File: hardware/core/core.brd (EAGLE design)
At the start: 159.7 x 189.2 mm, 710 parts, among them IC1 MAX481CSA, IC10 MAX481CSA, IC11 MAX481CSA, IC12 MAX481CSA, IC13 MAX481CSA, IC14 MAX481CSA, IC15 MAX481CSA, IC16 MAX481CSA, IC17 MAX481CSA, IC18 MAX481CSA, IC19 MAX481CSA, IC2 LD117AS12TR, IC20 MAX481CSA, IC21 MAX481CSA, IC22 LD117AS12TR, IC3 MAX481CSA, IC4 MAX481CSA, IC5 MAX481CSA, IC6 MAX481CSA, IC7 MAX481CSA, IC8 MAX481CSA, IC9 MAX481CSA, U1 6N138SDM

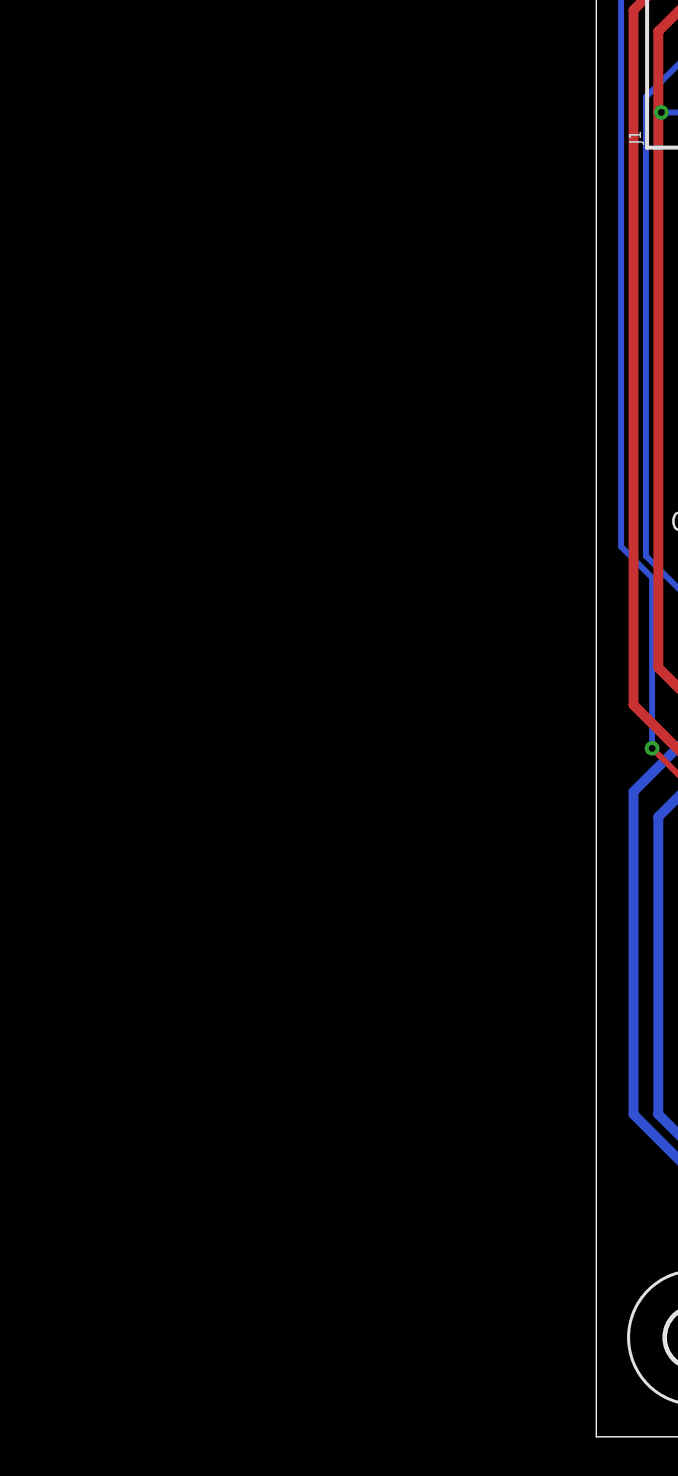
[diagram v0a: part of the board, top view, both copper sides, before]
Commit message: add esp32-s3
(for future use)
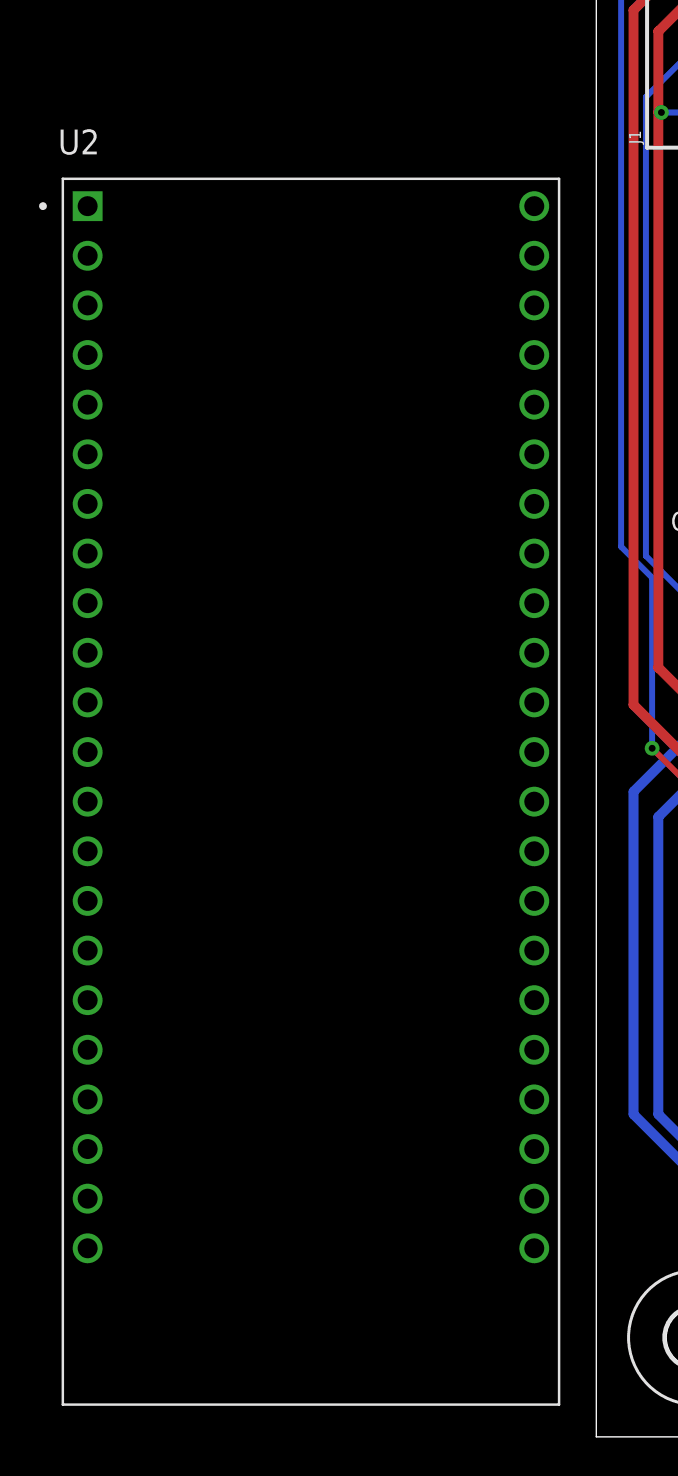
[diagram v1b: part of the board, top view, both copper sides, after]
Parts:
- added U2: ESP32-S3-DEVKITC-1-N8R2, ESP32-S3-DEVKITC-1-N8R2:XCVR_ESP32-S3-DEVKITC-1-N8R2
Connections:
- new net 3V3: U2.J1_1, U2.J1_2
- new net 5V0: U2.J1_21
- net GND: now also U2.J1_22, U2.J3_1, U2.J3_21, U2.J3_22

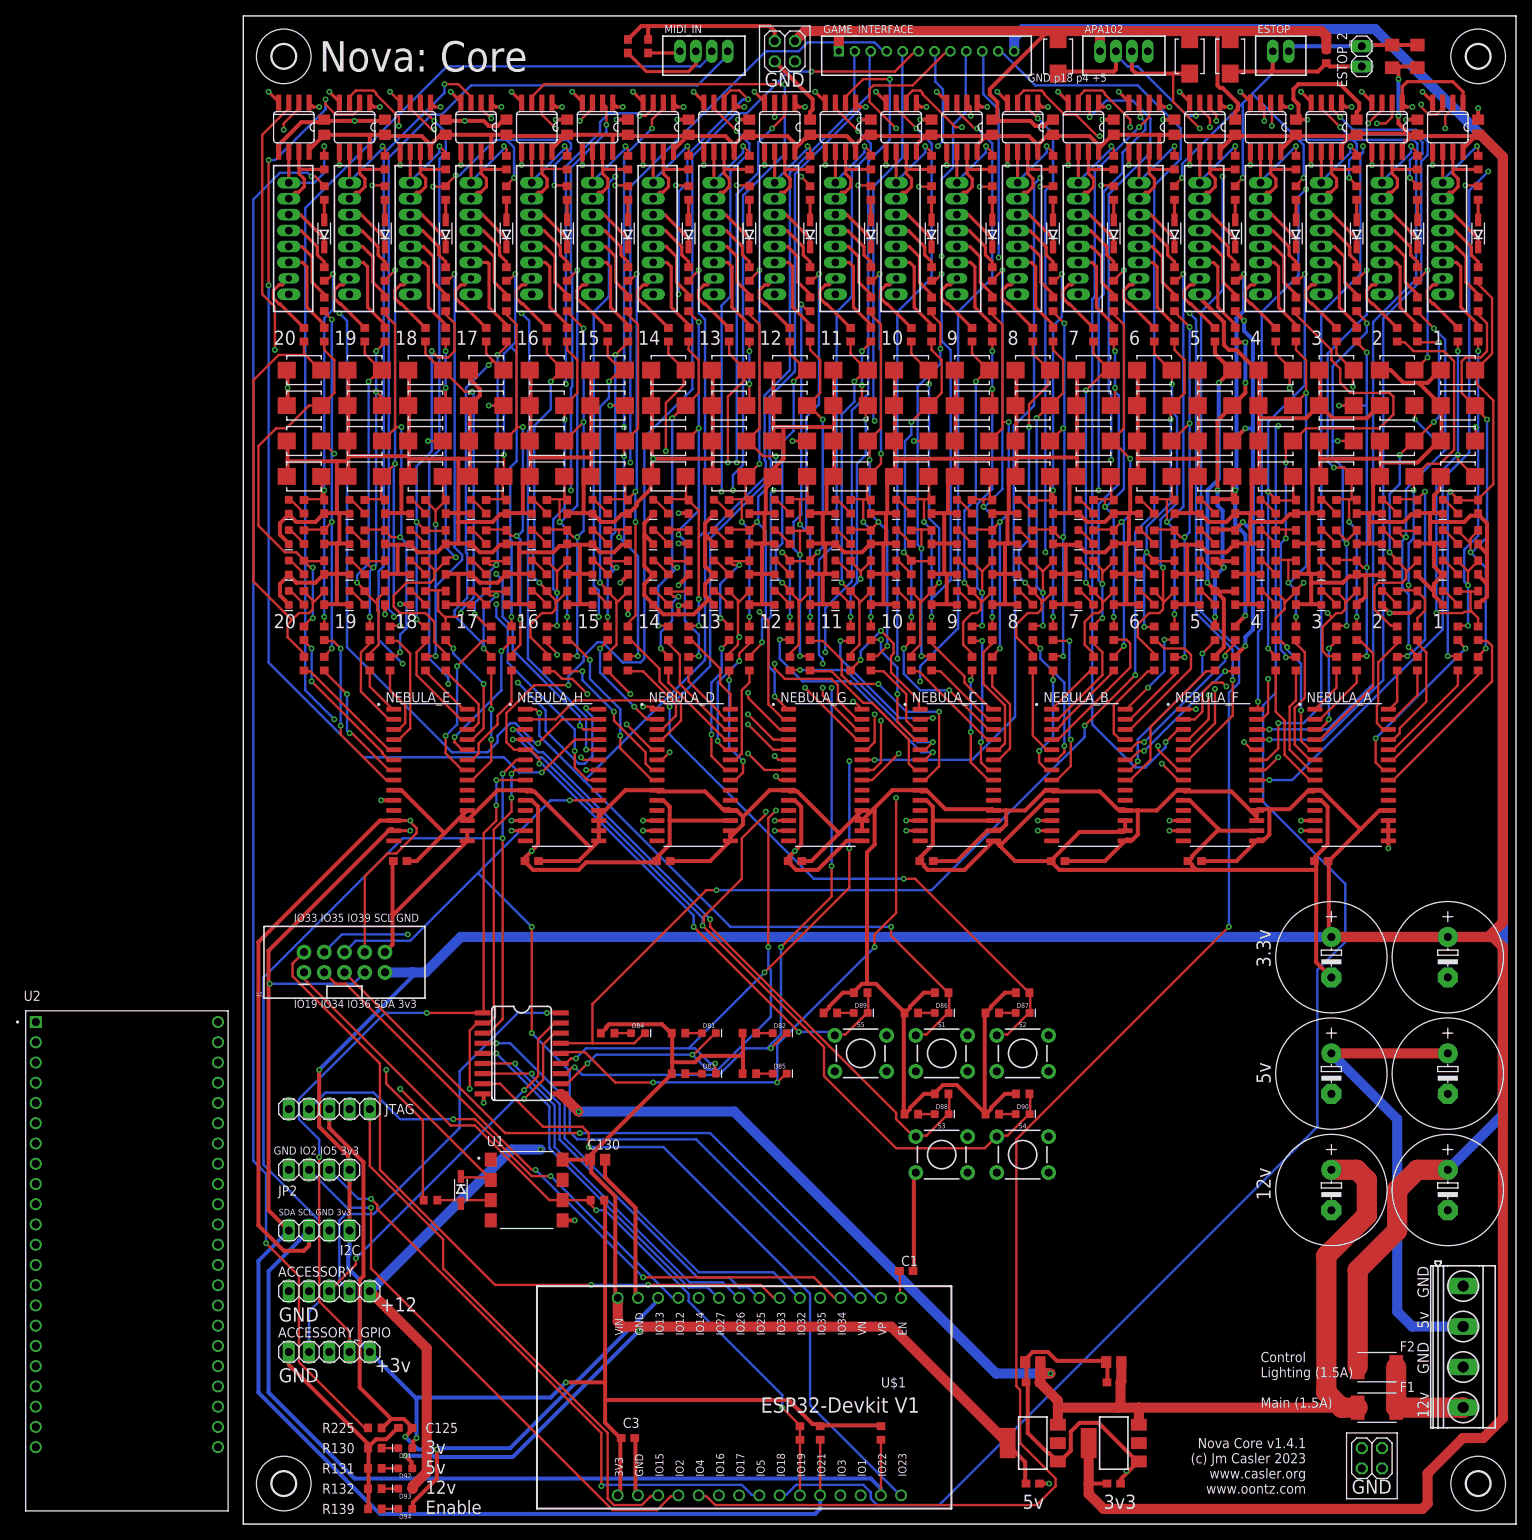
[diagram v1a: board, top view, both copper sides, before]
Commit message: re & de status LEDs added
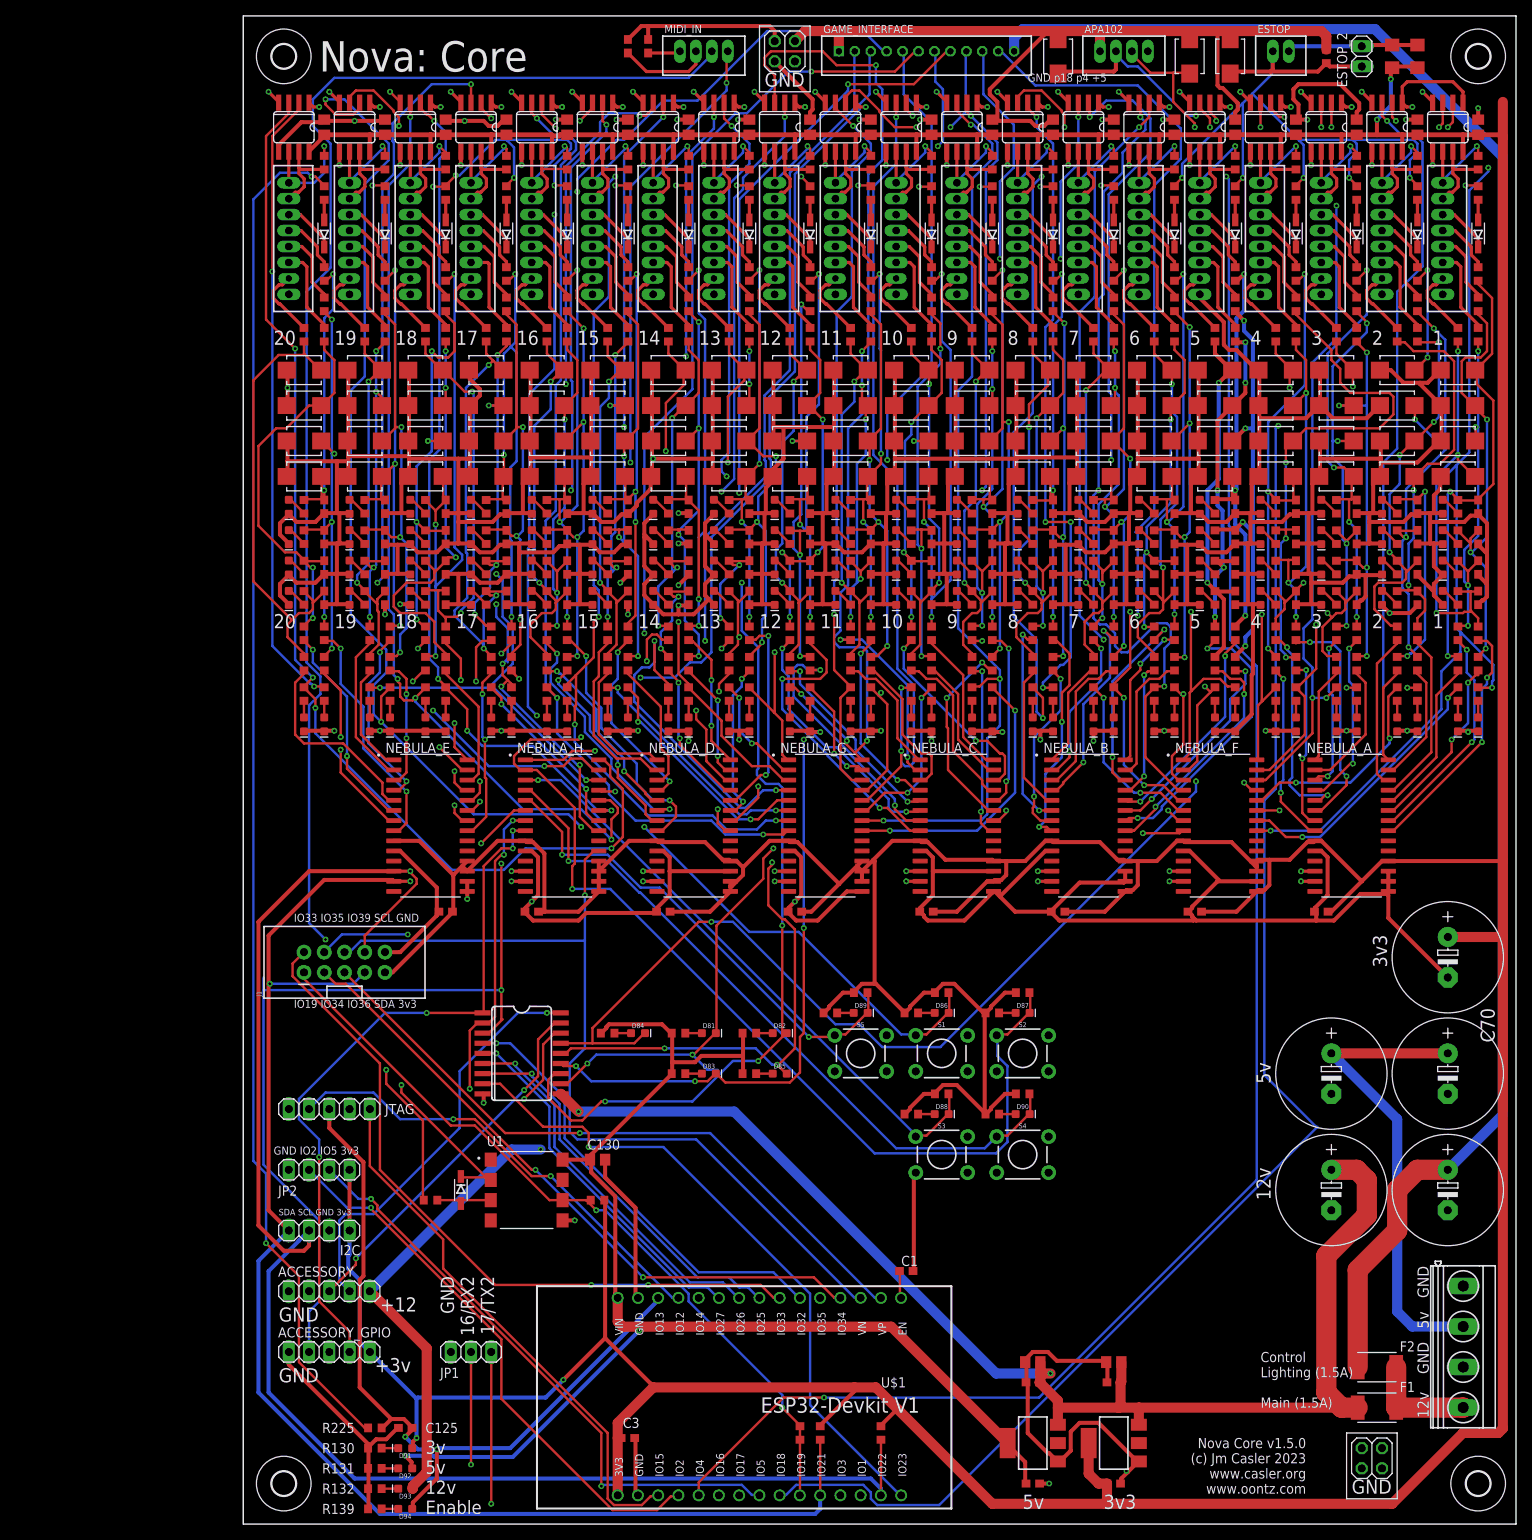
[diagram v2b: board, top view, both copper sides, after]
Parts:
- removed C72: 2200uf, rcl:E5-13
- removed U2: ESP32-S3-DEVKITC-1-N8R2, ESP32-S3-DEVKITC-1-N8R2:XCVR_ESP32-S3-DEVKITC-1-N8R2
- added D199, D200, D201, D202, D203, D204, D205, D206, D207, D208, D209, D210, D211, D212, D213, D214, D215, D216, D217, D218, D219, D220, D221, D222, D223, D224, D225, D226, D227, D228, D229, D230, D231, D232, D233, D234, D235, D236, D237, D238: (no value), SparkFun-LED:LED-0603
- added JP1: (no value), pinhead:1X03
- added R308, R309, R311, R312, R313, R314, R315, R316, R317, R318, R319, R320, R321, R322, R323, R324, R325, R326, R327, R328, R329, R330, R331, R332, R333, R334, R335, R336, R337, R338, R339, R340, R341, R342, R343, R344, R345, R346, R347, R348: 1k, rcl:R0603
- C69, C70, C71: value 2200uf -> 470uf
- moved C7 8.54 mm to (25.4, 76.8)
- moved C10 6.35 mm to (102.2, 76.8)
- moved C11 6.35 mm to (52.7, 76.8)
- moved C12 6.35 mm to (119.4, 76.8)
- moved C13 6.35 mm to (69.2, 76.8)
- moved C34 6.35 mm to (36.2, 76.8)
- moved C8 6.35 mm to (135.3, 76.8)
- moved C9 6.35 mm to (85.7, 76.8)
- moved NEBULA_A 6.35 mm to (139.1, 87.6)
- moved NEBULA_B 6.35 mm to (106.0, 87.6)
- moved NEBULA_C 6.35 mm to (89.5, 87.6)
- moved NEBULA_D 6.35 mm to (56.5, 87.6)
- moved NEBULA_E 6.35 mm to (23.5, 87.6)
- moved NEBULA_F 6.35 mm to (122.6, 87.6)
- moved NEBULA_G 6.35 mm to (73.0, 87.6)
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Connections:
- removed net 16: IC1.1, IC10.1, IC11.1, IC12.1, IC13.1, IC14.1, IC15.1, IC16.1, IC17.1, IC18.1, IC19.1, IC20.1, IC21.1, IC3.1, IC4.1, IC5.1, IC6.1, IC7.1, IC8.1, IC9.1, U$1.6
- removed net 17: IC1.4, IC10.4, IC11.4, IC12.4, IC13.4, IC14.4, IC15.4, IC16.4, IC17.4, IC18.4, IC19.4, IC20.4, IC21.4, IC3.4, IC4.4, IC5.4, IC6.4, IC7.4, IC8.4, IC9.4, U$1.7
- removed net 3V3: U2.J1_1, U2.J1_2
- removed net 5V0: U2.J1_21
- new net 16/RX2: IC1.1, IC10.1, IC11.1, IC12.1, IC13.1, IC14.1, IC15.1, IC16.1, IC17.1, IC18.1, IC19.1, IC20.1, IC21.1, IC3.1, IC4.1, IC5.1, IC6.1, IC7.1, IC8.1, IC9.1, JP1.2, U$1.6
- new net 17/TX2: IC1.4, IC10.4, IC11.4, IC12.4, IC13.4, IC14.4, IC15.4, IC16.4, IC17.4, IC18.4, IC19.4, IC20.4, IC21.4, IC3.4, IC4.4, IC5.4, IC6.4, IC7.4, IC8.4, IC9.4, JP1.3, U$1.7
- new net N$350: D200.A, R309.2
- new net N$351: D201.A, R311.2
- new net N$354: D202.A, R312.2
- new net N$355: D203.A, R313.2
- new net N$356: D204.A, R314.2
- new net N$357: D205.A, R315.2
- new net N$358: D206.A, R316.2
- new net N$359: D207.A, R317.2
- new net N$360: D208.A, R318.2
- new net N$361: D209.A, R319.2
- new net N$362: D210.A, R320.2
- new net N$363: D211.A, R321.2
- new net N$364: D212.A, R322.2
- new net N$365: D213.A, R323.2
- new net N$366: D214.A, R324.2
- new net N$367: D215.A, R325.2
- new net N$368: D216.A, R326.2
- new net N$369: D217.A, R327.2
- new net N$370: D218.A, R328.2
- new net N$371: D219.A, R329.2
- new net N$372: D220.A, R330.2
- new net N$373: D221.A, R331.2
- new net N$374: D222.A, R332.2
- new net N$375: D223.A, R333.2
- new net N$376: D224.A, R334.2
- new net N$377: D225.A, R335.2
- new net N$378: D226.A, R336.2
- new net N$379: D227.A, R337.2
- new net N$380: D228.A, R338.2
- new net N$381: D229.A, R339.2
- new net N$382: D230.A, R340.2
- new net N$383: D231.A, R341.2
- new net N$384: D232.A, R342.2
- new net N$385: D233.A, R343.2
- new net N$386: D234.A, R344.2
- new net N$387: D235.A, R345.2
- new net N$388: D236.A, R346.2
- new net N$389: D237.A, R347.2
- new net N$390: D238.A, R348.2
- new net N$84: D199.A, R308.2
- net +3V3: no longer C72.+
- net F0: now also R309.1
- net F1: now also R308.1
- net F10: now also R320.1
- net F11: now also R319.1
- net F12: now also R322.1
- net F13: now also R321.1
- net F14: now also R324.1
- net F15: now also R323.1
- net F2: now also R312.1
- net F3: now also R311.1
- net F4: now also R314.1
- net F5: now also R313.1
- net F6: now also R316.1
- net F7: now also R315.1
- net F8: now also R318.1
- net F9: now also R317.1
- net G0: now also R326.1
- net G1: now also R325.1
- net G10: now also R336.1
- net G11: now also R335.1
- net G12: now also R338.1
- net G13: now also R337.1
- net G14: now also R340.1
- net G15: now also R339.1
- net G2: now also R328.1
- net G3: now also R327.1
- net G4: now also R330.1
- net G5: now also R329.1
- net G6: now also R332.1
- net G7: now also R331.1
- net G8: now also R334.1
- net G9: now also R333.1
- net GND: now also D199.C, D200.C, D201.C, D202.C, D203.C, D204.C, D205.C, D206.C, D207.C, D208.C, D209.C, D210.C, D211.C, D212.C, D213.C, D214.C, D215.C, D216.C, D217.C, D218.C, D219.C, D220.C, D221.C, D222.C, D223.C, D224.C, D225.C, D226.C, D227.C, D228.C, D229.C, D230.C, D231.C, D232.C, D233.C, D234.C, D235.C, D236.C, D237.C, D238.C, JP1.1; no longer C72.-, U2.J1_22, U2.J3_1, U2.J3_21, U2.J3_22
- net H0: now also R342.1
- net H1: now also R341.1
- net H2: now also R344.1
- net H3: now also R343.1
- net H4: now also R346.1
- net H5: now also R345.1
- net H6: now also R348.1
- net H7: now also R347.1
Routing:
- net 17/TX2: track 0.00 -> 433.6 mm, vias 0 -> 21
- net 16/RX2: track 0.00 -> 423.0 mm, vias 0 -> 20
- net 17: track 414.4 -> 0.00 mm, vias 20 -> 0
- net 16: track 408.7 -> 0.00 mm, vias 19 -> 0
- net +3V3: track 1109.0 -> 959.6 mm, vias 5 -> 4
- net GND: track 1628.4 -> 1725.0 mm, vias 51 -> 67
- net H9: track 182.4 -> 226.4 mm, vias 2 -> 3
- net H7: track 110.9 -> 142.5 mm, vias 3 -> 4
- net N$59: track 199.9 -> 229.8 mm
- net F0: track 102.3 -> 131.7 mm, vias 3 -> 4
- net H3: track 92.2 -> 119.6 mm, vias 3 -> 4
- net F3: track 89.4 -> 113.5 mm, vias 2 -> 3
- net H5: track 97.1 -> 120.9 mm, vias 3 -> 4
- net G0: track 92.1 -> 115.9 mm, vias 2 -> 4
- net G7: track 103.9 -> 127.6 mm, vias 2 -> 4
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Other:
- board text added: "GND 16/RX2 17/TX2"
- board text added: "Nova Core v1.5.0 (c) Jm Casler 2023 www.casler.org www.oontz.com"
- board text removed: "3.3v"
- board text removed: "Nova Core v1.4.1 (c) Jm Casler 2023 www.casler.org www.oontz.com"
